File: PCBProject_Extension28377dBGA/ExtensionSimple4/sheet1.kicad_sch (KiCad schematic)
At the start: 150 parts, among them J1 Conn_02x05_Odd_Even, J2 Conn_02x05_Odd_Even, Q1 FMMT618TA, U1 SN74ABT541, U2 SN74ABT541, U3 SN74ABT541, U4 SN74ABT541

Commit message: add I2C2 and SPI B
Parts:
- added DC_BUS_2M3, DC_BUS_2M4, GND_2M3, GND_2M4: ${MANUFACTURER PART}, TestPoint:TestPoint_Pad_1.0x1.0mm, symbol sheet1-altium-import:root_1_TP-黄色测试点
- added I2C2: Conn_02x05_Odd_Even, Connector_PinHeader_2.54mm:PinHeader_2x05_P2.54mm_Vertical, symbol Connector_Generic:Conn_02x05_Odd_Even
- renumbered J2 to I2C1
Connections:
- net SPI B MI HS is gone; now on net SPI_B_MI_HS: DSP1.147 (147_GP64)
- net SPI B MO HS is gone; now on net SPI_B_MO_HS: DSP1.145 (145_GP63)
- net AGND: now also I2C2.10 (Pin_10), I2C2.3 (Pin_3), I2C2.4 (Pin_4), I2C2.9 (Pin_9)
- net VDD: now also I2C2.1 (Pin_1), I2C2.2 (Pin_2)
- net at C19.1, N1.9, R47.1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: now also GND_2M3.1
- net at C20.1, N1.13, R49.1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: now also GND_2M4.1
- net at C17.2, N1.10, R46.1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: now also DC_BUS_2M3.1
- net at C18.2, N1.12, R48.1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: now also DC_BUS_2M4.1
- net MSCLB: now reaches DSP1.116 (A3_116)
- net MSCLB: now also I2C2.5 (Pin_5), I2C2.6 (Pin_6)
- net MSDAB: now reaches DSP1.118 (A2_118)
- net MSDAB: now also I2C2.7 (Pin_7), I2C2.8 (Pin_8)
- no-connect marks 91 -> 85
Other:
- note added: "GP31"
- note added: "GP37"
- note added: "GP40"
- note added: "GP41"
- note added: "GP48"
- note added: "GP49"
- note added: "GP80"
- note added: "GP81"
- note removed: "GP104"
- note removed: "GP105"
- note removed: "GP106"
- note removed: "GP107"
- moved on the sheet: R46, R47, R49, SPI1

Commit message: add 12 LTC6240HV
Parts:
- removed RU3, RU4, RU5, RU6: DNP, Resistor_SMD:R_0805_2012Metric, symbol sheet1-altium-import:root_0_Res2
- added A1 (x4), A3 (x4), A6 (x4): LTC6240HV, SamacSys_Parts:SOT95P280X100-5N, symbol SensorLEM-altium-import:root_0_AO_LTC6240HV
- added C1 (x4), C10 (x4), C18 (x4), C20 (x4), C27 (x4), C9 (x4): 105, Capacitor_SMD:C_0805_2012Metric, symbol SensorLEM-altium-import:root_2_Cap
- added C11 (x4), C16 (x4), C2 (x4), C21 (x4), C26 (x4), C6 (x4): 103, Capacitor_SMD:C_0805_2012Metric, symbol SensorLEM-altium-import:root_2_Cap
- added C12 (x4), C23 (x4), C3 (x4): 101, Capacitor_SMD:C_0805_2012Metric, symbol SensorLEM-altium-import:root_1_Cap
- added C13 (x4), C25 (x4), C4 (x4): 103, Capacitor_SMD:C_0805_2012Metric, symbol SensorLEM-altium-import:root_1_Cap
- added C28, C29: 106 25V, 1mmlab_footprint:1206 (钽电容), symbol SensorLEM-altium-import:root_3_Cap Pol3
- added C30, C31: 104, Capacitor_SMD:C_0805_2012Metric, symbol SensorLEM-altium-import:root_1_Cap Semi
- added R10 (x4), R14 (x4), R18 (x4), R21 (x4), R3 (x4), R7 (x4): 10k, Resistor_SMD:R_0805_2012Metric, symbol SensorLEM-altium-import:root_0_Res2
- added R11 (x4), R19 (x4), R4 (x4): 470R, Resistor_SMD:R_0805_2012Metric, symbol SensorLEM-altium-import:root_2_Res2
- added R13 (x4), R17 (x4), R2 (x4), R20 (x4), R5 (x4), R9 (x4): 20k, Resistor_SMD:R_0805_2012Metric, symbol SensorLEM-altium-import:root_0_Res2
- added RB1 (x4), RB4 (x4), RB9 (x4): 0R, Resistor_SMD:R_0805_2012Metric, symbol SensorLEM-altium-import:root_0_Res2
- added RM1 (x4), RM2 (x4), RM3 (x4): 24R 1%精度, Resistor_SMD:R_2512_6332Metric, symbol SensorLEM-altium-import:root_3_Res2
- added RU1 (x4), RU2 (x4), RU3 (x4): DNP, Resistor_SMD:R_0805_2012Metric, symbol SensorLEM-altium-import:root_0_Res2
- added U1: ADR423ARZ, 1mmlab_footprint:SOIC-8, symbol SensorLEM-altium-import:root_0_ADR423ARZ
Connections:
- net +12: now also IPM-LEM1.18, IPM-LEM2.18, IPM-LEM3.18, IPM-LEM4.18; no longer IPM-LEM1.16, IPM-LEM2.16, IPM-LEM3.16, IPM-LEM4.16
- net -12: now also IPM-LEM1.17, IPM-LEM2.17, IPM-LEM3.17, IPM-LEM4.17; no longer IPM-LEM1.15, IPM-LEM2.15, IPM-LEM3.15, IPM-LEM4.15
- net 12VGND: now also IPM-LEM1.15, IPM-LEM2.15, IPM-LEM3.15, IPM-LEM4.15, R13.1, R13.1, R13.1, R13.1, R20.1, R20.1, R20.1, R20.1, R5.1, R5.1, R5.1, R5.1, RM1.2, RM1.2, RM1.2, RM1.2, RM2.2, RM2.2, RM2.2, RM2.2, RM3.2, RM3.2, RM3.2, RM3.2
- net A+5V: now also A1.5 (Vcc), A1.5 (Vcc), A1.5 (Vcc), A1.5 (Vcc), A3.5 (Vcc), A3.5 (Vcc), A3.5 (Vcc), A3.5 (Vcc), A6.5 (Vcc), A6.5 (Vcc), A6.5 (Vcc), A6.5 (Vcc), C1.2, C1.2, C1.2, C1.2, C10.2, C10.2, C10.2, C10.2, C11.2, C11.2, C11.2, C11.2, C2.2, C2.2, C2.2, C2.2, C20.2, C20.2, C20.2, C20.2, C21.2, C21.2, C21.2, C21.2, C28.1, C30.2, U1.2 (VIN); no longer IPM-LEM1.18, IPM-LEM2.18, IPM-LEM3.18, IPM-LEM4.18
- net A-5V: now also A1.2 (Vee), A1.2 (Vee), A1.2 (Vee), A1.2 (Vee), A3.2 (Vee), A3.2 (Vee), A3.2 (Vee), A3.2 (Vee), A6.2 (Vee), A6.2 (Vee), A6.2 (Vee), A6.2 (Vee), C16.2, C16.2, C16.2, C16.2, C18.2, C18.2, C18.2, C18.2, C26.2, C26.2, C26.2, C26.2, C27.2, C27.2, C27.2, C27.2, C6.2, C6.2, C6.2, C6.2, C9.2, C9.2, C9.2, C9.2; no longer IPM-LEM1.17, IPM-LEM2.17, IPM-LEM3.17, IPM-LEM4.17
- net AGND: now also C1.1, C1.1, C1.1, C1.1, C10.1, C10.1, C10.1, C10.1, C11.1, C11.1, C11.1, C11.1, C12.2, C12.2, C12.2, C12.2, C13.1, C13.1, C13.1, C13.1, C16.1, C16.1, C16.1, C16.1, C18.1, C18.1, C18.1, C18.1, C2.1, C2.1, C2.1, C2.1, C20.1, C20.1, C20.1, C20.1, C21.1, C21.1, C21.1, C21.1, C23.2, C23.2, C23.2, C23.2, C25.1, C25.1, C25.1, C25.1, C26.1, C26.1, C26.1, C26.1, C27.1, C27.1, C27.1, C27.1, C28.2, C29.2, C3.2, C3.2, C3.2, C3.2, C30.1, C31.1, C4.1, C4.1, C4.1, C4.1, C6.1, C6.1, C6.1, C6.1, C9.1, C9.1, C9.1, C9.1, RU1.2, RU1.2, RU1.2, RU1.2, RU2.2, RU2.2, RU2.2, RU2.2, RU3.2, RU3.2, RU3.2, RU3.2, U1.4 (GND)
- net D12V1: now also IPM-LEM1.16, IPM-LEM2.16, IPM-LEM3.16, IPM-LEM4.16
- net IPM_IU1: now also C25.2, R19.1; no longer IPM-LEM1.5
- net IPM_IU2: now also C25.2, R19.1; no longer IPM-LEM2.5
- net IPM_IU3: now also C25.2, R19.1; no longer IPM-LEM3.5
- net IPM_IU4: now also C25.2, R19.1; no longer IPM-LEM4.5
- net IPM_IV1: now also C13.2, R11.1; no longer IPM-LEM1.3
- net IPM_IV2: now also C13.2, R11.1; no longer IPM-LEM2.3
- net IPM_IV3: now also C13.2, R11.1; no longer IPM-LEM3.3
- net IPM_IV4: now also C13.2, R11.1; no longer IPM-LEM4.3
- net IPM_IW1: now also C4.2, R4.1; no longer IPM-LEM1.1
- net IPM_IW2: now also C4.2, R4.1; no longer IPM-LEM2.1
- net IPM_IW3: now also C4.2, R4.1; no longer IPM-LEM3.1
- net IPM_IW4: now also C4.2, R4.1; no longer IPM-LEM4.1
- net REF_3V: now also C29.1, C31.2, RB1.1, RB1.1, RB1.1, RB1.1, RB4.1, RB4.1, RB4.1, RB4.1, RB9.1, RB9.1, RB9.1, RB9.1, U1.6 (VOUT)
- new net: R9.1, RB4.2, RU2.1 (x4)
- new net: A3.3 (+IN), C12.1, R10.2, R9.2 (x4)
- new net: A3.1 (out), R11.2, R14.1 (x4)
- new net: A3.4 (-IN), R13.2, R14.2 (x4)
- new net: R17.1, RB9.2, RU3.1 (x4)
- new net: A6.3 (+IN), C23.1, R17.2, R18.2 (x4)
- new net: R2.1, RB1.2, RU1.1 (x4)
- new net: A1.3 (+IN), C3.1, R2.2, R3.2 (x4)
- new net: A1.1 (out), R4.2, R7.1 (x4)
- new net: A6.1 (out), R19.2, R21.1 (x4)
- new net: A6.4 (-IN), R20.2, R21.2 (x4)
- new net: A1.4 (-IN), R5.2, R7.2 (x4)
- new net CSO1_1: IPM-LEM1.1, R3.1, RM1.1
- new net CSO1_2: IPM-LEM1.3, R10.1, RM2.1
- new net CSO1_3: IPM-LEM1.5, R18.1, RM3.1
- new net CSO2_1: IPM-LEM2.1, R3.1, RM1.1
- new net CSO2_2: IPM-LEM2.3, R10.1, RM2.1
- new net CSO2_3: IPM-LEM2.5, R18.1, RM3.1
- new net CSO3_1: IPM-LEM3.1, R3.1, RM1.1
- new net CSO3_2: IPM-LEM3.3, R10.1, RM2.1
- new net CSO3_3: IPM-LEM3.5, R18.1, RM3.1
- new net CSO4_1: IPM-LEM4.1, R3.1, RM1.1
- new net CSO4_2: IPM-LEM4.3, R10.1, RM2.1
- new net CSO4_3: IPM-LEM4.5, R18.1, RM3.1
- no-connect marks 85 -> 91
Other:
- note added: "1.5V offset"

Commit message: fix SCI_C and D, add ECAP to 1TO4, but 1TO4 haven't finish.
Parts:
- added ECAP1, ECAP2: Conn_01x06, Connector_PinHeader_2.54mm:PinHeader_1x06_P2.54mm_Vertical, symbol Connector_Generic:Conn_01x06
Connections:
- net A+5V: now also ECAP1.4 (Pin_4), ECAP2.4 (Pin_4)
- net AGND: now also ECAP1.6 (Pin_6), ECAP2.6 (Pin_6)
- net ECAP1_IPM_TerminalDutyU1: now also ECAP1.1 (Pin_1)
- net ECAP2_IPM_TerminalDutyV1: now also ECAP1.2 (Pin_2)
- net ECAP3_IPM_TerminalDutyW1: now also ECAP1.3 (Pin_3)
- net ECAP4_IPM_TerminalDutyU2: now also ECAP2.1 (Pin_1)
- net ECAP5_IPM_TerminalDutyV2: now also ECAP2.2 (Pin_2)
- net ECAP6_IPM_TerminalDutyW2: now also ECAP2.3 (Pin_3)
- net UART_SCI_RXDC: now also DSP1.120 (A1_120); no longer DSP1.107 (107_D3)
- net UART_SCI_RXDD: now also DSP1.108 (A7_108); no longer DSP1.105 (105_D4)
- net UART_SCI_TXDC: now also DSP1.122 (A0_122); no longer DSP1.106 (A8_106)
- net UART_SCI_TXDD: now also DSP1.110 (A6_110); no longer DSP1.104 (A9_104)
- net VDD: now also ECAP1.5 (Pin_5), ECAP2.5 (Pin_5)
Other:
- note added: "ECAP"
- note added: "GP38"
- note added: "GP39"
- note added: "GP46"
- note added: "GP47"
- note removed: "GP48"
- note removed: "GP49"
- note removed: "GP80"
- note removed: "GP81"

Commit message: 修改UVW顺序
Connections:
- net IPM_IU1: now also C4.2, R4.1; no longer C25.2, R19.1
- net IPM_IU2: now also C4.2, R4.1; no longer C25.2, R19.1
- net IPM_IU3: now also C4.2, R4.1; no longer C25.2, R19.1
- net IPM_IU4: now also C4.2, R4.1; no longer C25.2, R19.1
- net IPM_IW1: now also C25.2, R19.1; no longer C4.2, R4.1
- net IPM_IW2: now also C25.2, R19.1; no longer C4.2, R4.1
- net IPM_IW3: now also C25.2, R19.1; no longer C4.2, R4.1
- net IPM_IW4: now also C25.2, R19.1; no longer C4.2, R4.1
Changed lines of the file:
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@@
     (effects (font (size 1.27 1.27)) (justify left bottom))
   )
-  (label "IPM_IW1" (at 449.58 411.48 180) (fields_autoplaced)
+  (label "IPM_IU1" (at 449.58 411.48 180) (fields_autoplaced)
     (effects (font (size 1.27 1.27)) (justify left bottom))
   )
@@
     (effects (font (size 1.27 1.27)) (justify left bottom))
   )
-  (label "IPM_IU4" (at 93.98 552.45 180) (fields_autoplaced)
+  (label "IPM_IW4" (at 93.98 552.45 180) (fields_autoplaced)
     (effects (font (size 1.27 1.27)) (justify left bottom))
   )
@@
     (effects (font (size 1.27 1.27)) (justify left bottom))
   )
-  (label "IPM_IU2" (at 317.5 549.91 180) (fields_autoplaced)
+  (label "IPM_IW2" (at 317.5 549.91 180) (fields_autoplaced)
     (effects (font (size 1.27 1.27)) (justify left bottom))
   )
@@
     (effects (font (size 1.27 1.27)) (justify left bottom))
   )
-  (label "IPM_IU1" (at 433.07 551.18 180) (fields_autoplaced)
+  (label "IPM_IW1" (at 433.07 551.18 180) (fields_autoplaced)
     (effects (font (size 1.27 1.27)) (justify left bottom))
   )
@@
     (effects (font (size 1.27 1.27)) (justify left bottom))
   )
-  (label "IPM_IW3" (at 219.71 411.48 180) (fields_autoplaced)
+  (label "IPM_IU3" (at 219.71 411.48 180) (fields_autoplaced)
     (effects (font (size 1.27 1.27)) (justify left bottom))
   )
@@
     (effects (font (size 1.27 1.27)) (justify left bottom))
   )
-  (label "IPM_IW2" (at 334.01 410.21 180) (fields_autoplaced)
+  (label "IPM_IU2" (at 334.01 410.21 180) (fields_autoplaced)
     (effects (font (size 1.27 1.27)) (justify left bottom))
   )
@@
     (effects (font (size 1.27 1.27)) (justify left bottom))
   )
-  (label "IPM_IW4" (at 106.68 412.75 180) (fields_autoplaced)
+  (label "IPM_IU4" (at 106.68 412.75 180) (fields_autoplaced)
     (effects (font (size 1.27 1.27)) (justify left bottom))
   )
@@
     (effects (font (size 1.27 1.27)) (justify left bottom))
   )
-  (label "IPM_IU3" (at 203.2 551.18 180) (fields_autoplaced)
-    (effects (font (size 1.27 1.27)) (justify left bottom))
-  )
+  (label "IPM_IW3" (at 203.2 551.18 180) (fields_autoplaced)
+    (effects (font (size 1.27 1.27)) (justify left bottom))
+  )

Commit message: modified uvw
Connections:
- no-connect marks 91 -> 90
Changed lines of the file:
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@@
   (no_connect (at 642.62 314.96))
   (no_connect (at 688.34 414.02))
-  (no_connect (at 722.249 339.344))
   (no_connect (at 276.86 588.1878))
   (no_connect (at 979.17 781.05))

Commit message: fomula four2one, but the signal of current sensor is not good.
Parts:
- added C100, C101, C99: 103, Capacitor_SMD:C_0805_2012Metric, symbol sheet1-altium-import:root_3_Cap
- added DI2, DI3, DI4: Conn_02x02_Counter_Clockwise, Connector_PinSocket_2.54mm:PinSocket_2x02_P2.54mm_Vertical, symbol Connector_Generic:Conn_02x02_Counter_Clockwise
- added J2, J3, J4: Conn_02x05_Odd_Even, Connector_IDC:IDC-Header_2x05_P2.54mm_Vertical, symbol Connector_Generic:Conn_02x05_Odd_Even
- added R116, R118, R120: 100R, Resistor_SMD:R_0805_2012Metric, symbol sheet1-altium-import:root_2_Res2
- added R117, R119, R121: 1K, Resistor_SMD:R_0805_2012Metric, symbol sheet1-altium-import:root_1_Res2
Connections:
- net AGND: now also C100.1, C101.1, C99.1, DI2.2 (Pin_2), DI3.2 (Pin_2), DI4.2 (Pin_2), J2.9 (Pin_9), J3.9 (Pin_9), J4.9 (Pin_9), R117.2, R119.2, R121.2
- net D+5V: now also J2.10 (Pin_10), J3.10 (Pin_10), J4.10 (Pin_10)
- net DI-2-DSP-3.3V: now also C101.2, R120.1, R121.1
- net MQEP3A: now also J3.2 (Pin_2)
- net MQEP3B: now also J3.4 (Pin_4)
- net MQEP3Z: now also J3.6 (Pin_6)
- net PE_GND: now also J2.7 (Pin_7), J3.7 (Pin_7), J4.7 (Pin_7)
- net QEP2_HALL_U: now also DSP3.67 (67_GP127), J2.1 (Pin_1); no longer DSP3.68 (GP115_68)
- net QEP2_HALL_W: now also DSP3.63 (63_GP131), J2.5 (Pin_5); no longer DSP3.64 (GP67_64)
- net QEP3_HALL_U: now also J3.1 (Pin_1)
- net QEP3_HALL_V: now also J3.3 (Pin_3)
- net QEP3_HALL_W: now also J3.5 (Pin_5)
- net VDD: now also DI2.1 (Pin_1), DI3.1 (Pin_1), DI4.1 (Pin_1), J2.8 (Pin_8), J3.8 (Pin_8), J4.8 (Pin_8)
- net DI-3-DSP-3.3V: now reaches DSP1.91 (91_D11)
- net DI-3-DSP-3.3V: now also C99.2, R116.1, R117.1
- net DI-4-DSP-3.3V: now reaches DSP1.93 (93_D10)
- net DI-4-DSP-3.3V: now also C100.2, R118.1, R119.1
- net MQEP2A: now reaches DSP3.53 (53_GP100)
- net MQEP2A: now also J2.2 (Pin_2)
- net MQEP2Z: now reaches DSP3.54 (GP103_54)
- net MQEP2Z: now also J2.6 (Pin_6)
- net MQEP2S: now reaches DSP3.55 (55_GP102)
- net MQEP2B: now reaches DSP3.56 (GP101_56)
- net MQEP2B: now also J2.4 (Pin_4)
- net QEP2_HALL_V: now reaches DSP3.65 (65_GP116)
- net QEP2_HALL_V: now also J2.3 (Pin_3)
- net QEP4_HALL_U: now reaches DSP3.69 (69_GP128)
- net QEP4_HALL_U: now also J4.1 (Pin_1)
- net QEP4_HALL_V: now reaches DSP3.71 (71_GP126)
- net QEP4_HALL_V: now also J4.3 (Pin_3)
- net QEP4_HALL_W: now reaches DSP3.73 (73_GP95)
- net QEP4_HALL_W: now also J4.5 (Pin_5)
- new net: DI4.3 (Pin_3), DI4.4 (Pin_4), R120.2
- new net: DI3.3 (Pin_3), DI3.4 (Pin_4), R118.2
- new net: DI2.3 (Pin_3), DI2.4 (Pin_4), R116.2
- no-connect marks 90 -> 85
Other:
- moved on the sheet: C7, DI1, J1, R28, R29

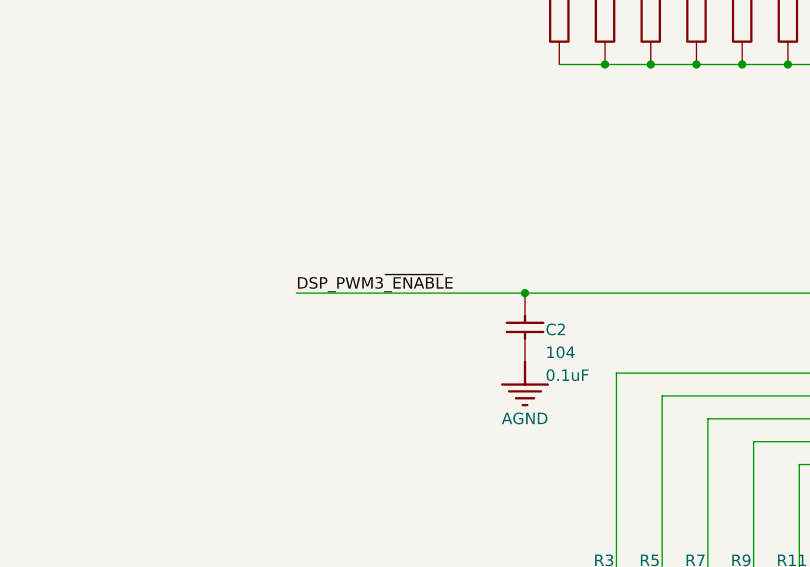
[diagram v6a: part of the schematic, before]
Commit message: 重定义了DAC接口和修复了底板的PWM的bug，还需实现DAC电源集成
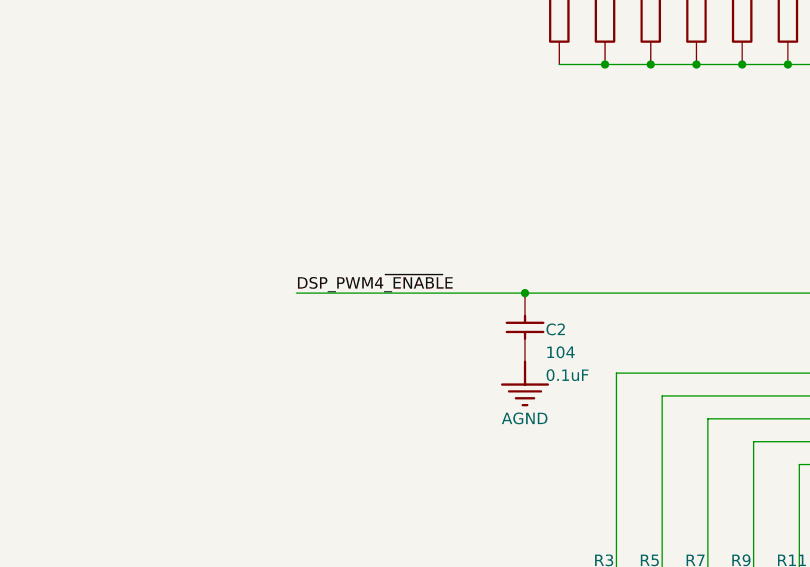
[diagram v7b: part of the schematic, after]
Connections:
- net DSP_PWM3~{_ENABL}E: no longer C2.2, U2.1 (*OE1), U2.19 (*OE2)
- net DSP_PWM4~{_ENABL}E: now also C2.2, U2.1 (*OE1), U2.19 (*OE2)
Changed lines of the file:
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@@
     (effects (font (size 1.27 1.27)) (justify left bottom))
   )
-  (label "DSP_PWM3~{_ENABL}E" (at 280.67 745.49 180) (fields_autoplaced)
+  (label "DSP_PWM4~{_ENABL}E" (at 280.67 745.49 180) (fields_autoplaced)
     (effects (font (size 1.27 1.27)) (justify left bottom))
   )

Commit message: 377新板子暂停
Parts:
- renumbered A6 to A1, A6 to A10, A1 to A11, A3 to A12, A1 to A2, A6 to A4, A1 to A5, A3 to A6, A6 to A7, A1 to A8, A3 to A9, C30 to C23, C23 to C24, C28 to C25, C3 to C26, C12 to C27, C21 to C28, C26 to C29, C2 to C30, C6 to C31, C11 to C32, C16 to C33, C20 to C34, C27 to C35, C31 to C36, C1 to C37, C9 to C38, C10 to C39, C18 to C40, C25 to C41, C29 to C42, C4 to C43, C13 to C44, C23 to C45, C3 to C46, C12 to C47, C21 to C48, C26 to C49, C2 to C50, C6 to C51, C11 to C52, C16 to C53, C20 to C54, C27 to C55, C1 to C56, C9 to C57, C10 to C58, C18 to C59, C25 to C60, C4 to C61, C13 to C62, C23 to C63, C3 to C64, C12 to C65, C21 to C66, C26 to C67, C2 to C68, C6 to C69, C11 to C70, C16 to C71, C20 to C72, C27 to C73, C1 to C74, C9 to C75, C10 to C76, C18 to C77, C25 to C78, C4 to C79, C13 to C80, C23 to C81, C3 to C82, C12 to C83, C21 to C84, C26 to C85, C2 to C86, C6 to C87, C11 to C88, C16 to C89, C20 to C90, C27 to C91, C1 to C92, C9 to C93, C10 to C94, C18 to C95, C25 to C96, C4 to C97, C13 to C98, R11 to R100, R17 to R101, R18 to R102, R20 to R103, R21 to R104, R2 to R105, R3 to R106, R5 to R107, R7 to R108, R9 to R109, R10 to R110, R13 to R111, R14 to R112, R19 to R113, R4 to R114, R11 to R115, R17 to R56, R18 to R57, R20 to R58, R21 to R59, R2 to R60, R3 to R61, R5 to R62, R7 to R63, R9 to R64, R10 to R65, R13 to R66, R14 to R67, R19 to R68, R4 to R69, R11 to R70, R17 to R71, R18 to R72, R20 to R73, R21 to R74, R2 to R75, R3 to R76, R5 to R77, R7 to R78, R9 to R79, R10 to R80, R13 to R81, R14 to R82, R19 to R83, R4 to R84, R11 to R85, R17 to R86, R18 to R87, R20 to R88, R21 to R89, R2 to R90, R3 to R91, R5 to R92, R7 to R93, R9 to R94, R10 to R95, R13 to R96, R14 to R97, R19 to R98, R4 to R99, RB9 to RB1, RB9 to RB10, RB1 to RB11, RB4 to RB12, RB1 to RB2, RB4 to RB3, RB9 to RB4, RB1 to RB5, RB4 to RB6, RB9 to RB7, RB1 to RB8, RB4 to RB9, RM3 to RM1, RM3 to RM10, RM1 to RM11, RM2 to RM12, RM1 to RM2, RM2 to RM3, RM3 to RM4, RM1 to RM5, RM2 to RM6, RM3 to RM7, RM1 to RM8, RM2 to RM9, RU3 to RU10, RU1 to RU11, RU2 to RU12, RU3 to RU13, RU1 to RU14, RU2 to RU15, RU3 to RU16, RU1 to RU17, RU2 to RU18, RU3 to RU7, RU1 to RU8, RU2 to RU9, U1 to U5
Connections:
- net UART_SCI_RXDD: now also DSP1.110 (A6_110); no longer DSP1.108 (A7_108)
- net UART_SCI_TXDD: now also DSP1.108 (A7_108); no longer DSP1.110 (A6_110)
